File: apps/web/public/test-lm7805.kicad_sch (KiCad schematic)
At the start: 5 parts, among them J1 VIN_CONN, J2 VOUT_5V, U1 LM7805

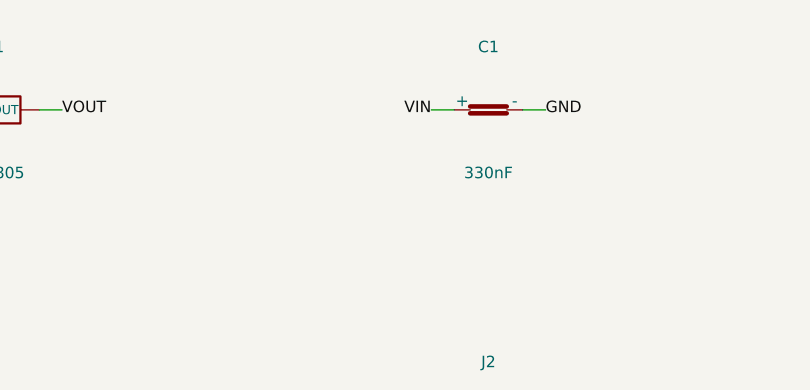
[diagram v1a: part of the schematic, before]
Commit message: fix(viewer): correct title block detection and paper height formula
- JS: TITLE_HEIGHT=43mm (fixed KiCad value, not 30% ratio) + dual-constraint
  cy = min(maxCy_frame, maxCy_title) guarantees frame visible + title hidden
- JS: waitAndZoom triggers on symbols OR net_labels (handles no-label schematics)
- Python: paper_h = component_bottom_y + 6mm gap + 44mm title block (replaces
  broken TITLE_RATIO=0.30 formula that left zero gap before title block)
- Regenerated test schematics: LM7805 (115mm), NE555 (150mm), ESP32 (150mm)
- Verified all 3 tabs: frame visible, all components shown, title block hidden
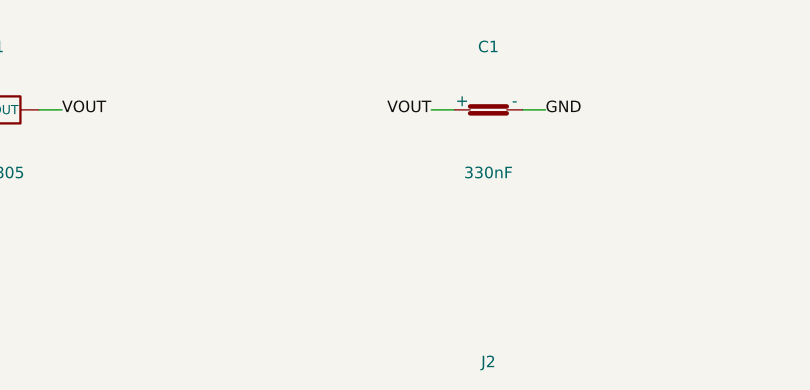
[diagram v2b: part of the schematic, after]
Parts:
- C1, C2: footprint Capacitor_THT:C_Disc_D5.0mm_W2.5mm_P5.00mm -> 0402
- J1, J2: footprint Connector_PinHeader_2.54mm:PinHeader_1x02_P2.54mm_Vertical -> Connector_PinHeader_2.54mm:PinHeader_1x02
- U1: footprint Package_TO_SOT_THT:TO-220-3_Vertical -> SOT-223
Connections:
- net VIN: no longer C1.1 (+)
- net VOUT: now also C1.1 (+)
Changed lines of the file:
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@@
 (kicad_sch (version 20230121) (generator "layrix-circuit-synth")
-  (paper "User" 149 93)
+  (paper "User" 149 115)
   (symbol (lib_id "Device:VReg_3Pin") (at 12 12 0) (unit 1) (in_bom yes) (on_board yes)
     (property "Reference" "U1" (at 12 5 0) (effects (font (size 1.27 1.27)) (justify center)))
     (property "Value" "LM7805" (at 12 19 0) (effects (font (size 1.27 1.27)) (justify center)))
-    (property "Footprint" "Package_TO_SOT_THT:TO-220-3_Vertical" (at 12 22 0) (effects (font (size 1.27 1.27)) (hide yes)))
+    (property "Footprint" "SOT-223" (at 12 22 0) (effects (font (size 1.27 1.27)) (hide yes)))
   )
   (symbol (lib_id "Device:C") (at 67 12 0) (unit 1) (in_bom yes) (on_board yes)
     (property "Reference" "C1" (at 67 5 0) (effects (font (size 1.27 1.27)) (justify center)))
     (property "Value" "330nF" (at 67 19 0) (effects (font (size 1.27 1.27)) (justify center)))
-    (property "Footprint" "Capacitor_THT:C_Disc_D5.0mm_W2.5mm_P5.00mm" (at 67 22 0) (effects (font (size 1.27 1.27)) (hide yes)))
+    (property "Footprint" "0402" (at 67 22 0) (effects (font (size 1.27 1.27)) (hide yes)))
   )
   (symbol (lib_id "Device:C") (at 122 12 0) (unit 1) (in_bom yes) (on_board yes)
     (property "Reference" "C2" (at 122 5 0) (effects (font (size 1.27 1.27)) (justify center)))
     (property "Value" "100nF" (at 122 19 0) (effects (font (size 1.27 1.27)) (justify center)))
-    (property "Footprint" "Capacitor_THT:C_Disc_D5.0mm_W2.5mm_P5.00mm" (at 122 22 0) (effects (font (size 1.27 1.27)) (hide yes)))
+    (property "Footprint" "0402" (at 122 22 0) (effects (font (size 1.27 1.27)) (hide yes)))
   )
   (symbol (lib_id "Connector_Generic:Conn_01x02") (at 12 47 0) (unit 1) (in_bom yes) (on_board yes)
     (property "Reference" "J1" (at 12 40 0) (effects (font (size 1.27 1.27)) (justify center)))
     (property "Value" "VIN_CONN" (at 12 54 0) (effects (font (size 1.27 1.27)) (justify center)))
-    (property "Footprint" "Connector_PinHeader_2.54mm:PinHeader_1x02_P2.54mm_Vertical" (at 12 57 0) (effects (font (size 1.27 1.27)) (hide yes)))
+    (property "Footprint" "Connector_PinHeader_2.54mm:PinHeader_1x02" (at 12 57 0) (effects (font (size 1.27 1.27)) (hide yes)))
   )
   (symbol (lib_id "Connector_Generic:Conn_01x02") (at 67 47 0) (unit 1) (in_bom yes) (on_board yes)
     (property "Reference" "J2" (at 67 40 0) (effects (font (size 1.27 1.27)) (justify center)))
     (property "Value" "VOUT_5V" (at 67 54 0) (effects (font (size 1.27 1.27)) (justify center)))
-    (property "Footprint" "Connector_PinHeader_2.54mm:PinHeader_1x02_P2.54mm_Vertical" (at 67 57 0) (effects (font (size 1.27 1.27)) (hide yes)))
+    (property "Footprint" "Connector_PinHeader_2.54mm:PinHeader_1x02" (at 67 57 0) (effects (font (size 1.27 1.27)) (hide yes)))
   )
+  (wire (pts (xy 8.19 47.0) (xy 5.65 47.0)) (stroke (width 0.1524) (type default)))
+  (label "VIN" (at 5.65 47.0 180) (effects (font (size 1.27 1.27))))
   (wire (pts (xy 6.92 12.0) (xy 4.38 12.0)) (stroke (width 0.1524) (type default)))
   (label "VIN" (at 4.38 12.0 180) (effects (font (size 1.27 1.27))))
-  (wire (pts (xy 63.19 12.0) (xy 60.65 12.0)) (stroke (width 0.1524) (type default)))
-  (label "VIN" (at 60.65 12.0 180) (effects (font (size 1.27 1.27))))
-  (wire (pts (xy 8.19 47.0) (xy 5.65 47.0)) (stroke (width 0.1524) (type default)))
-  (label "VIN" (at 5.65 47.0 180) (effects (font (size 1.27 1.27))))
+  (wire (pts (xy 15.81 47.0) (xy 18.35 47.0)) (stroke (width 0.1524) (type default)))
+  (label "GND" (at 18.35 47.0 0) (effects (font (size 1.27 1.27))))
   (wire (pts (xy 12.0 15.81) (xy 12.0 18.35)) (stroke (width 0.1524) (type default)))
   (label "GND" (at 12.0 18.35 90) (effects (font (size 1.27 1.27))))
+  (wire (pts (xy 70.81 47.0) (xy 73.35 47.0)) (stroke (width 0.1524) (type default)))
+  (label "GND" (at 73.35 47.0 0) (effects (font (size 1.27 1.27))))
   (wire (pts (xy 70.81 12.0) (xy 73.35 12.0)) (stroke (width 0.1524) (type default)))
   (label "GND" (at 73.35 12.0 0) (effects (font (size 1.27 1.27))))
   (wire (pts (xy 125.81 12.0) (xy 128.35 12.0)) (stroke (width 0.1524) (type default)))
   (label "GND" (at 128.35 12.0 0) (effects (font (size 1.27 1.27))))
-  (wire (pts (xy 15.81 47.0) (xy 18.35 47.0)) (stroke (width 0.1524) (type default)))
-  (label "GND" (at 18.35 47.0 0) (effects (font (size 1.27 1.27))))
-  (wire (pts (xy 70.81 47.0) (xy 73.35 47.0)) (stroke (width 0.1524) (type default)))
-  (label "GND" (at 73.35 47.0 0) (effects (font (size 1.27 1.27))))
   (wire (pts (xy 17.08 12.0) (xy 19.62 12.0)) (stroke (width 0.1524) (type default)))
   (label "VOUT" (at 19.62 12.0 0) (effects (font (size 1.27 1.27))))
+  (wire (pts (xy 63.19 47.0) (xy 60.65 47.0)) (stroke (width 0.1524) (type default)))
+  (label "VOUT" (at 60.65 47.0 180) (effects (font (size 1.27 1.27))))
+  (wire (pts (xy 63.19 12.0) (xy 60.65 12.0)) (stroke (width 0.1524) (type default)))
+  (label "VOUT" (at 60.65 12.0 180) (effects (font (size 1.27 1.27))))
   (wire (pts (xy 118.19 12.0) (xy 115.65 12.0)) (stroke (width 0.1524) (type default)))
   (label "VOUT" (at 115.65 12.0 180) (effects (font (size 1.27 1.27))))
-  (wire (pts (xy 63.19 47.0) (xy 60.65 47.0)) (stroke (width 0.1524) (type default)))
-  (label "VOUT" (at 60.65 47.0 180) (effects (font (size 1.27 1.27))))
   (sheet_instances (path "/" (page "1")))
 )

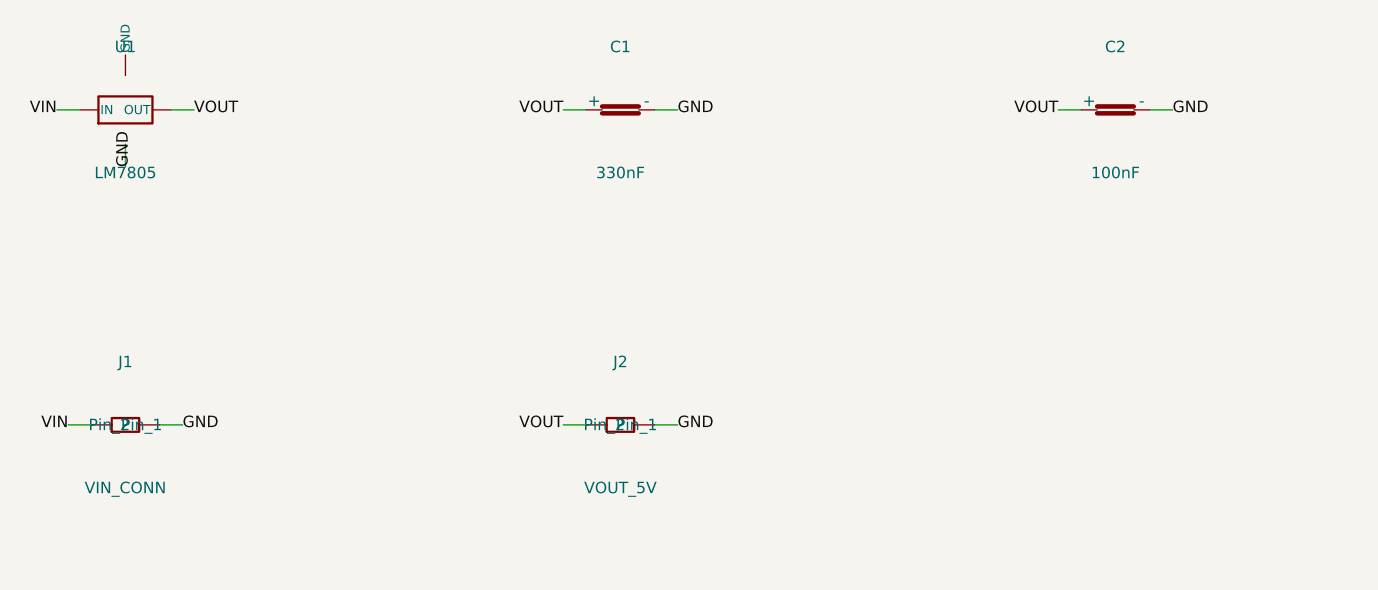
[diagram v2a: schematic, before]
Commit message: fix(layout): margin_top 12→20mm — composants 15mm du bord cadre interne
Composants étaient à y=12mm (7mm du bord interne), visuellement collés au cadre.
Maintenant à y=20mm (15mm de marge), clairement à l'intérieur du cadre.

- circuit_synth.py: margin_top = 20mm
- test-lm7805.kicad_sch: paper 149x123 (was 115)
- test-ne555.kicad_sch: paper 149x158 (was 150)
- test-esp32.kicad_sch: paper 149x158 (was 150)
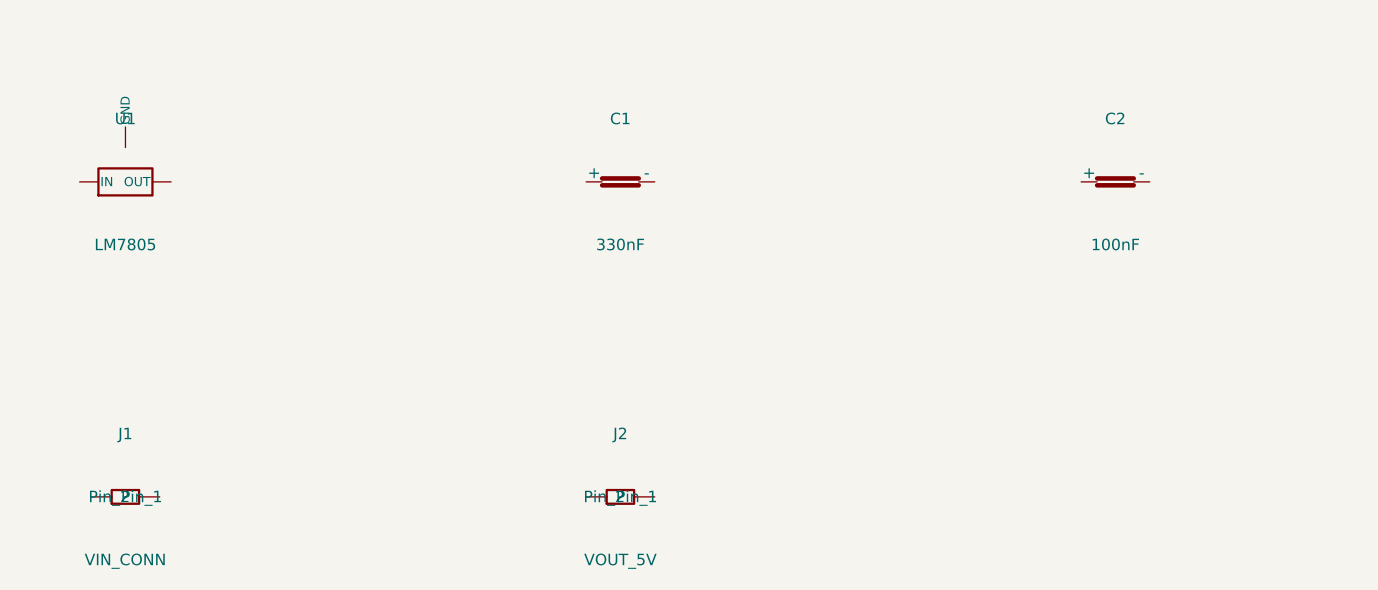
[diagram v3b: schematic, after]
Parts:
- C1, C2: footprint 0402 -> Capacitor_THT:C_Disc_D5.0mm_W2.5mm_P5.00mm
- J1, J2: footprint Connector_PinHeader_2.54mm:PinHeader_1x02 -> Connector_PinHeader_2.54mm:PinHeader_1x02_P2.54mm_Vertical
- U1: footprint SOT-223 -> Package_TO_SOT_THT:TO-220-3_Vertical
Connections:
- removed net GND: C1.2 (-), C2.2 (-), J1.2 (Pin_2), J2.2 (Pin_2)
- net VIN: no longer names the net of J1.1 (Pin_1)
- net VIN: no longer U1.1 (IN)
- removed net VOUT: C1.1 (+), C2.1 (+), J2.1 (Pin_1), U1.3 (OUT)
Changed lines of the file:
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@@
 (kicad_sch (version 20230121) (generator "layrix-circuit-synth")
-  (paper "User" 149 115)
-  (symbol (lib_id "Device:VReg_3Pin") (at 12 12 0) (unit 1) (in_bom yes) (on_board yes)
-    (property "Reference" "U1" (at 12 5 0) (effects (font (size 1.27 1.27)) (justify center)))
-    (property "Value" "LM7805" (at 12 19 0) (effects (font (size 1.27 1.27)) (justify center)))
-    (property "Footprint" "SOT-223" (at 12 22 0) (effects (font (size 1.27 1.27)) (hide yes)))
+  (paper "User" 149 123)
+  (symbol (lib_id "Device:VReg_3Pin") (at 12 20 0) (unit 1) (in_bom yes) (on_board yes)
+    (property "Reference" "U1" (at 12 13 0) (effects (font (size 1.27 1.27)) (justify center)))
+    (property "Value" "LM7805" (at 12 27 0) (effects (font (size 1.27 1.27)) (justify center)))
+    (property "Footprint" "Package_TO_SOT_THT:TO-220-3_Vertical" (at 12 30 0) (effects (font (size 1.27 1.27)) (hide yes)))
   )
-  (symbol (lib_id "Device:C") (at 67 12 0) (unit 1) (in_bom yes) (on_board yes)
-    (property "Reference" "C1" (at 67 5 0) (effects (font (size 1.27 1.27)) (justify center)))
-    (property "Value" "330nF" (at 67 19 0) (effects (font (size 1.27 1.27)) (justify center)))
-    (property "Footprint" "0402" (at 67 22 0) (effects (font (size 1.27 1.27)) (hide yes)))
+  (symbol (lib_id "Device:C") (at 67 20 0) (unit 1) (in_bom yes) (on_board yes)
+    (property "Reference" "C1" (at 67 13 0) (effects (font (size 1.27 1.27)) (justify center)))
+    (property "Value" "330nF" (at 67 27 0) (effects (font (size 1.27 1.27)) (justify center)))
+    (property "Footprint" "Capacitor_THT:C_Disc_D5.0mm_W2.5mm_P5.00mm" (at 67 30 0) (effects (font (size 1.27 1.27)) (hide yes)))
   )
-  (symbol (lib_id "Device:C") (at 122 12 0) (unit 1) (in_bom yes) (on_board yes)
-    (property "Reference" "C2" (at 122 5 0) (effects (font (size 1.27 1.27)) (justify center)))
-    (property "Value" "100nF" (at 122 19 0) (effects (font (size 1.27 1.27)) (justify center)))
-    (property "Footprint" "0402" (at 122 22 0) (effects (font (size 1.27 1.27)) (hide yes)))
+  (symbol (lib_id "Device:C") (at 122 20 0) (unit 1) (in_bom yes) (on_board yes)
+    (property "Reference" "C2" (at 122 13 0) (effects (font (size 1.27 1.27)) (justify center)))
+    (property "Value" "100nF" (at 122 27 0) (effects (font (size 1.27 1.27)) (justify center)))
+    (property "Footprint" "Capacitor_THT:C_Disc_D5.0mm_W2.5mm_P5.00mm" (at 122 30 0) (effects (font (size 1.27 1.27)) (hide yes)))
   )
-  (symbol (lib_id "Connector_Generic:Conn_01x02") (at 12 47 0) (unit 1) (in_bom yes) (on_board yes)
-    (property "Reference" "J1" (at 12 40 0) (effects (font (size 1.27 1.27)) (justify center)))
-    (property "Value" "VIN_CONN" (at 12 54 0) (effects (font (size 1.27 1.27)) (justify center)))
-    (property "Footprint" "Connector_PinHeader_2.54mm:PinHeader_1x02" (at 12 57 0) (effects (font (size 1.27 1.27)) (hide yes)))
+  (symbol (lib_id "Connector_Generic:Conn_01x02") (at 12 55 0) (unit 1) (in_bom yes) (on_board yes)
+    (property "Reference" "J1" (at 12 48 0) (effects (font (size 1.27 1.27)) (justify center)))
+    (property "Value" "VIN_CONN" (at 12 62 0) (effects (font (size 1.27 1.27)) (justify center)))
+    (property "Footprint" "Connector_PinHeader_2.54mm:PinHeader_1x02_P2.54mm_Vertical" (at 12 65 0) (effects (font (size 1.27 1.27)) (hide yes)))
   )
-  (symbol (lib_id "Connector_Generic:Conn_01x02") (at 67 47 0) (unit 1) (in_bom yes) (on_board yes)
-    (property "Reference" "J2" (at 67 40 0) (effects (font (size 1.27 1.27)) (justify center)))
-    (property "Value" "VOUT_5V" (at 67 54 0) (effects (font (size 1.27 1.27)) (justify center)))
-    (property "Footprint" "Connector_PinHeader_2.54mm:PinHeader_1x02" (at 67 57 0) (effects (font (size 1.27 1.27)) (hide yes)))
+  (symbol (lib_id "Connector_Generic:Conn_01x02") (at 67 55 0) (unit 1) (in_bom yes) (on_board yes)
+    (property "Reference" "J2" (at 67 48 0) (effects (font (size 1.27 1.27)) (justify center)))
+    (property "Value" "VOUT_5V" (at 67 62 0) (effects (font (size 1.27 1.27)) (justify center)))
+    (property "Footprint" "Connector_PinHeader_2.54mm:PinHeader_1x02_P2.54mm_Vertical" (at 67 65 0) (effects (font (size 1.27 1.27)) (hide yes)))
   )
-  (wire (pts (xy 8.19 47.0) (xy 5.65 47.0)) (stroke (width 0.1524) (type default)))
-  (label "VIN" (at 5.65 47.0 180) (effects (font (size 1.27 1.27))))
-  (wire (pts (xy 6.92 12.0) (xy 4.38 12.0)) (stroke (width 0.1524) (type default)))
-  (label "VIN" (at 4.38 12.0 180) (effects (font (size 1.27 1.27))))
-  (wire (pts (xy 15.81 47.0) (xy 18.35 47.0)) (stroke (width 0.1524) (type default)))
-  (label "GND" (at 18.35 47.0 0) (effects (font (size 1.27 1.27))))
-  (wire (pts (xy 12.0 15.81) (xy 12.0 18.35)) (stroke (width 0.1524) (type default)))
-  (label "GND" (at 12.0 18.35 90) (effects (font (size 1.27 1.27))))
-  (wire (pts (xy 70.81 47.0) (xy 73.35 47.0)) (stroke (width 0.1524) (type default)))
-  (label "GND" (at 73.35 47.0 0) (effects (font (size 1.27 1.27))))
-  (wire (pts (xy 70.81 12.0) (xy 73.35 12.0)) (stroke (width 0.1524) (type default)))
-  (label "GND" (at 73.35 12.0 0) (effects (font (size 1.27 1.27))))
-  (wire (pts (xy 125.81 12.0) (xy 128.35 12.0)) (stroke (width 0.1524) (type default)))
-  (label "GND" (at 128.35 12.0 0) (effects (font (size 1.27 1.27))))
-  (wire (pts (xy 17.08 12.0) (xy 19.62 12.0)) (stroke (width 0.1524) (type default)))
-  (label "VOUT" (at 19.62 12.0 0) (effects (font (size 1.27 1.27))))
-  (wire (pts (xy 63.19 47.0) (xy 60.65 47.0)) (stroke (width 0.1524) (type default)))
-  (label "VOUT" (at 60.65 47.0 180) (effects (font (size 1.27 1.27))))
-  (wire (pts (xy 63.19 12.0) (xy 60.65 12.0)) (stroke (width 0.1524) (type default)))
-  (label "VOUT" (at 60.65 12.0 180) (effects (font (size 1.27 1.27))))
-  (wire (pts (xy 118.19 12.0) (xy 115.65 12.0)) (stroke (width 0.1524) (type default)))
-  (label "VOUT" (at 115.65 12.0 180) (effects (font (size 1.27 1.27))))
   (sheet_instances (path "/" (page "1")))
 )
